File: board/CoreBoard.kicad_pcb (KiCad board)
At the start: 2 copper layers, 121.4 x 88.9 mm, 118 parts, among them J1 RJ45_LED_Shielded, J2 768250002, Q1 AO3401A, Q10 AO3401A, Q12 AO3401A, Q16 BSS138, Q17 BSS138, Q18 BSS138, Q2 AO3401A, Q3 AO3401A, Q4 AO3401A, Q5 AO3401A, Q6 AO3401A, Q7 AO3401A, Q8 AO3401A, Q9 AO3401A, SW11 SW_Wuerth_450301014042, SW12 SW_Wuerth_450301014042, SW13 SW_Wuerth_450301014042, SW14 SW_Wuerth_450301014042, SW15 SW_Wuerth_450301014042, SW16 SW_Wuerth_450301014042, SW4 SW_Push, SW6 SW_Push, SW7 SW_Push, SW8 SW_Push, U1 74VHC138FT, U2 OKI-78SR-12_1.0-W36H-C, U3 TPS54202DDCR, U4 GY-521, U5 Teensy4.1_DEV-16771, U6 MCP9808-E/MS, U7 OKI-78SR-5_1.5-W36H-C

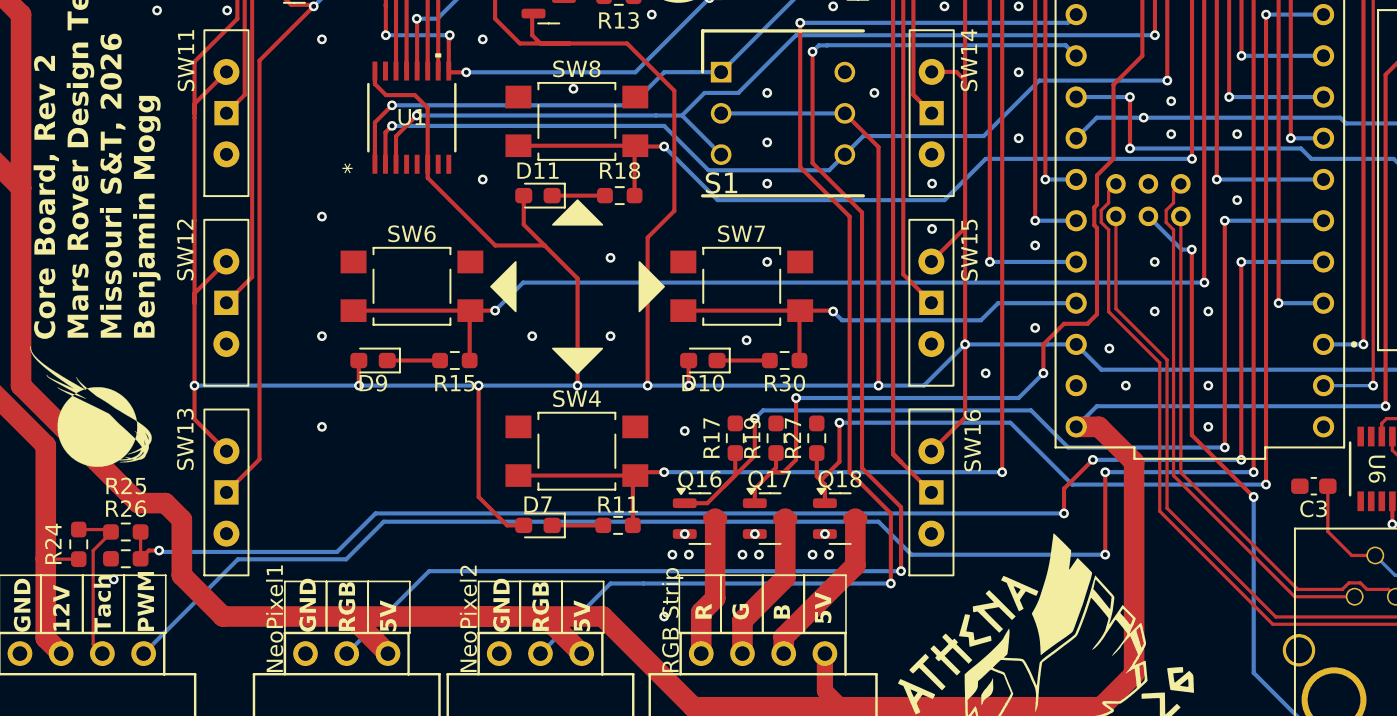
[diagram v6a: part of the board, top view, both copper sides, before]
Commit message: fix skew on ethernet diff pairs
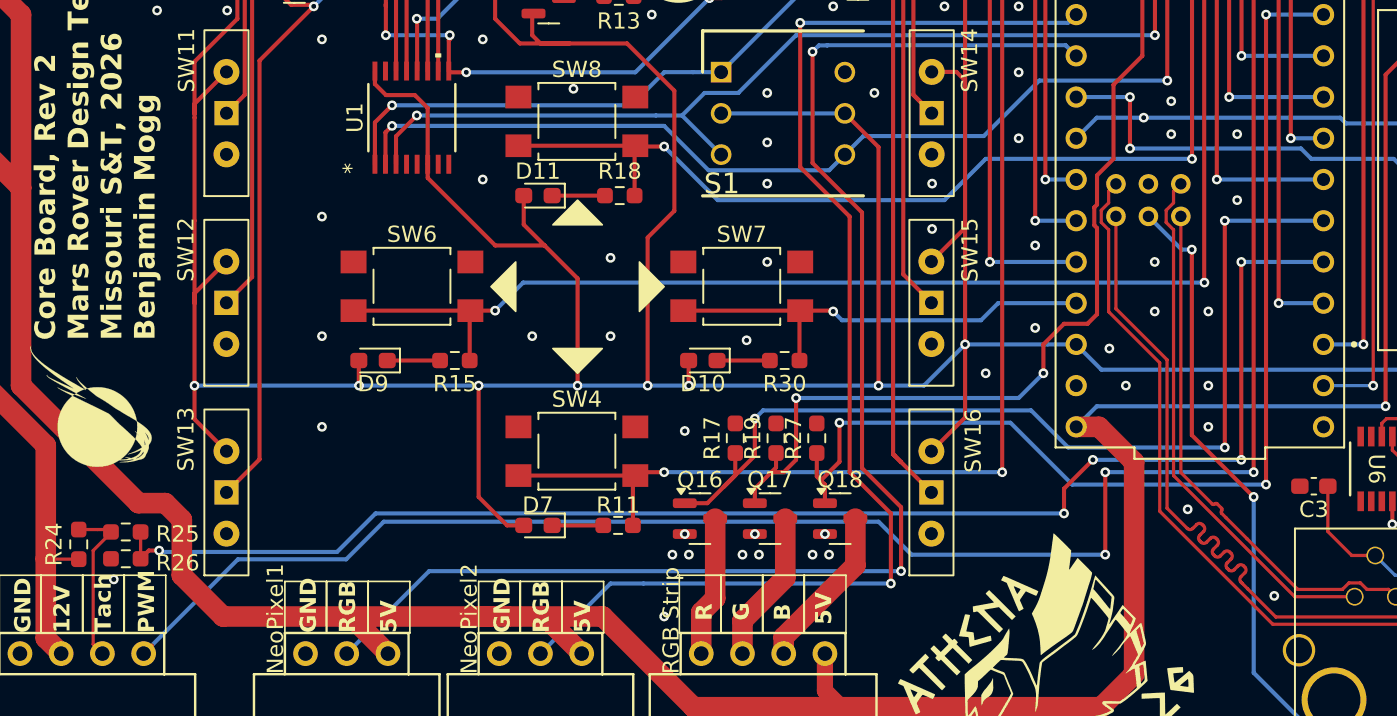
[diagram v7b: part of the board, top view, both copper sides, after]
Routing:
- net Rx+: track 40.6 -> 45.4 mm
- net GND: vias 102 -> 104
